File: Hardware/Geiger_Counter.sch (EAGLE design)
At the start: 55 parts, among them Q1 MPSA42, Q2 MPSA18, Q3 MMBT4403, Q4 MPSA18, U10 FT232RL-BASICSSOP, U17 AVR_SPI_PRG_6PTH, U7 TRANSFORMERAUDIO, U8 ATMEGA168, X1 USBSMD

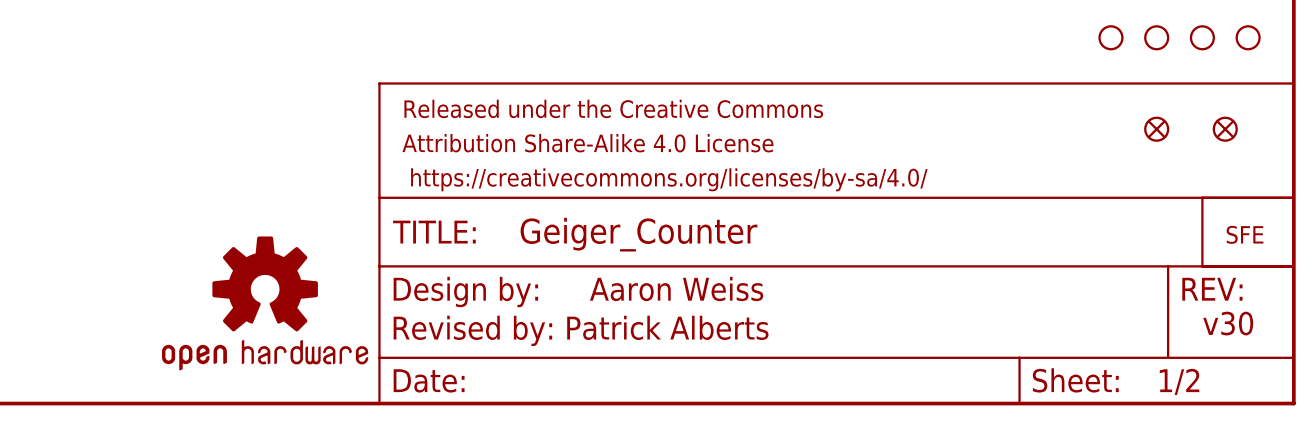
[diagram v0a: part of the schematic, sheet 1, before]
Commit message: Updated trace sizes and silk
1.) Updated silk to use non web logo.
2.) Fixed trace size continuities.
3.) Scooted LEDs and related resistors for better positioning.
4.) Couple of trace reroutes to be more efficient.
5.) Changed silk ratios from 18% to 15% to look cleaner.
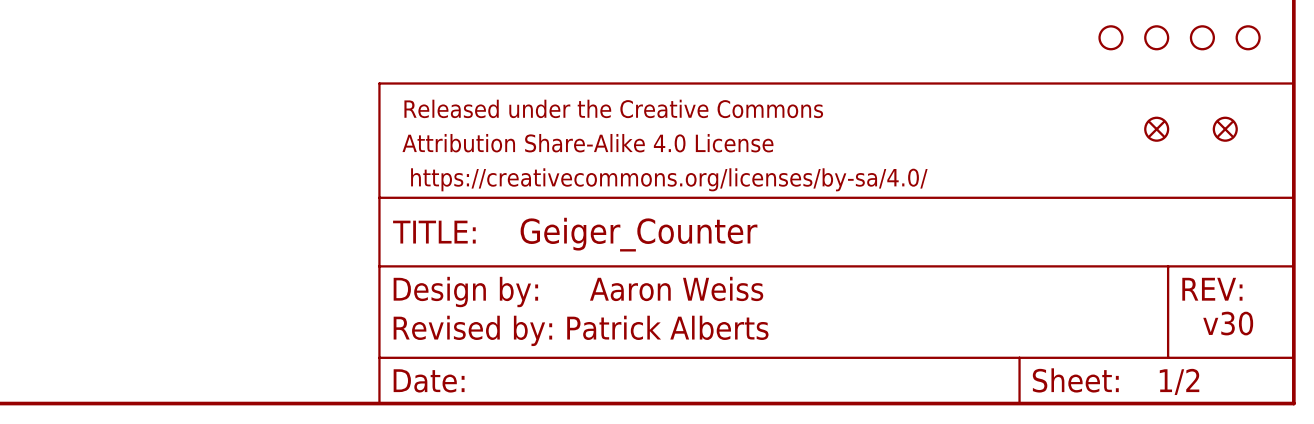
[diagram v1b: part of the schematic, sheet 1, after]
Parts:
- removed U$15: LOGO-SFENEW, SparkFun:LOGO-SFENEW
- removed U$5: OSHW-LOGOS, SparkFun:OSHW-LOGOS
- U8: value ATMEGA168 -> (none); device SparkFun:ATMEGA168 -> SparkFun-DigitalIC:ATMEGA328_SMT
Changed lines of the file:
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@@
 <?xml version="1.0" encoding="utf-8"?>
 <!DOCTYPE eagle SYSTEM "eagle.dtd">
-<eagle version="6.4">
+<eagle version="6.5.0">
 <drawing>
 <settings>
@@
 <part name="R8" library="SparkFun" deviceset="RESISTOR" device="AXIAL-0.3" value="10M"/>
 <part name="Q4" library="SparkFun" deviceset="TRANSISTOR_NPN" device="TO92" value="MPSA18"/>
-<part name="U$15" library="SparkFun" deviceset="LOGO-SFE" device="NEW"/>
 <part name="F1" library="SparkFun" deviceset="PTC" device="SMD"/>
 <part name="U$23" library="SparkFun" deviceset="5V" device=""/>
@@
 <part name="JP2" library="SparkFun" deviceset="M06" device="SIP" value="debug"/>
 <part name="S1" library="SparkFun" deviceset="SWITCH-DPDT" device="GPI"/>
-<part name="U$5" library="SparkFun" deviceset="OSHW-LOGO" device="S"/>
 <part name="FRAME2" library="SparkFun" deviceset="FRAME-LETTER" device=""/>
-<part name="U8" library="SparkFun" deviceset="ATMEGA168" device=""/>
+<part name="U8" library="SparkFun-DigitalIC" deviceset="ATMEGA328_SMT" device=""/>
 <part name="U$16" library="SparkFun" deviceset="5V" device=""/>
 <part name="R11" library="SparkFun-Resistors" deviceset="10KOHM1/10W1%(0603)" device="0603" value="10k"/>
@@
 </instance>
 <instance part="Q4" gate="G$1" x="114.3" y="111.76" rot="MR0"/>
-<instance part="U$15" gate="G$1" x="241.3" y="17.78"/>
 <instance part="F1" gate="G$1" x="63.5" y="43.18"/>
 <instance part="U$23" gate="G$1" x="35.56" y="48.26"/>
@@
 <instance part="JP2" gate="G$1" x="17.78" y="50.8"/>
 <instance part="S1" gate="G$1" x="50.8" y="43.18"/>
-<instance part="U$5" gate="G$1" x="134.62" y="12.7"/>
 <instance part="R14" gate="G$1" x="185.42" y="144.78" smashed="yes" rot="R270">
 <attribute name="NAME" x="186.9186" y="146.05" size="1.778" layer="95" rot="R270"/>

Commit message: Fixed traces and Schematic
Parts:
- added LOGO1: OSHW-LOGOM, SparkFun-Aesthetics:OSHW-LOGOM
- added LOGO2: SFE_LOGO_NAME_FLAME.1_INCH, SparkFun-Aesthetics:SFE_LOGO_NAME_FLAME.1_INCH
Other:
- moved on the sheet: F1, R6, S1

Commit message: Fixed 4wy Junc / Sch Flags
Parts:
- removed FRAME1: FRAME-LETTER, SparkFun-Aesthetics:FRAME-LETTER
- added FRAME2: FRAME-LEDGER, SparkFun-Aesthetics:FRAME-LEDGER
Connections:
- new net N$13: C7.2
- net GND: no longer C7.2
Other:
- note added: "v40"
- note removed: "v30"
